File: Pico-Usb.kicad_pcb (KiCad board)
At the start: 2 copper layers, 25 x 60 mm, 40 parts, among them J1 USB_A, J3 MEM2067-02-180-00-A_REVB, J4 10133475-10001LF, SW1 SW_Push, SW2 SW_Push, SW3 SW_Push, SW4 A6H-4101, U1 RP2040, U2 W25Q128JVS, U3 MAX40200AUK, U4 MAX40200AUK, U5 AP2112K-3.3, U6 TS3USB221ARSER, Y2 ABM3B-12.000MHZ-10-1-U-T

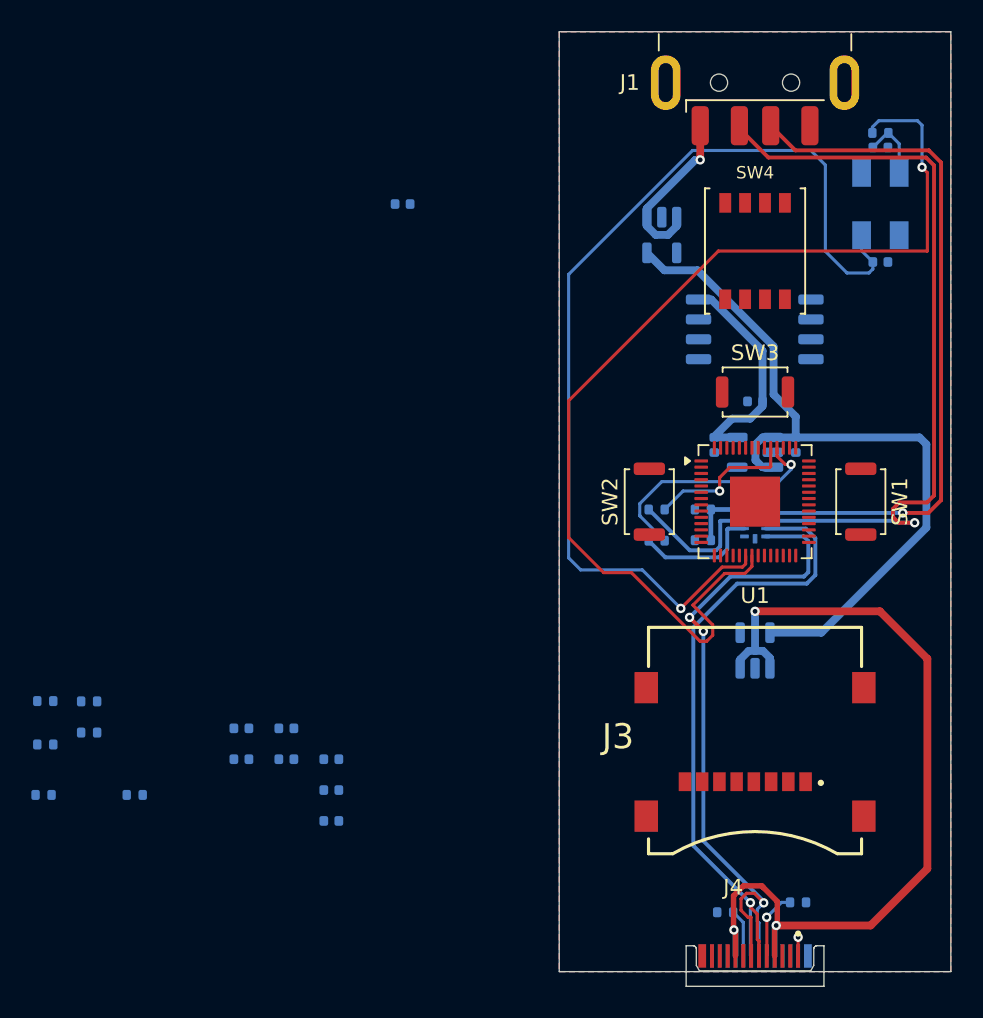
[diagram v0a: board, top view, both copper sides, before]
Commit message: Corregi el posicionamiento usb y mejore un poco la distribución de las pistas
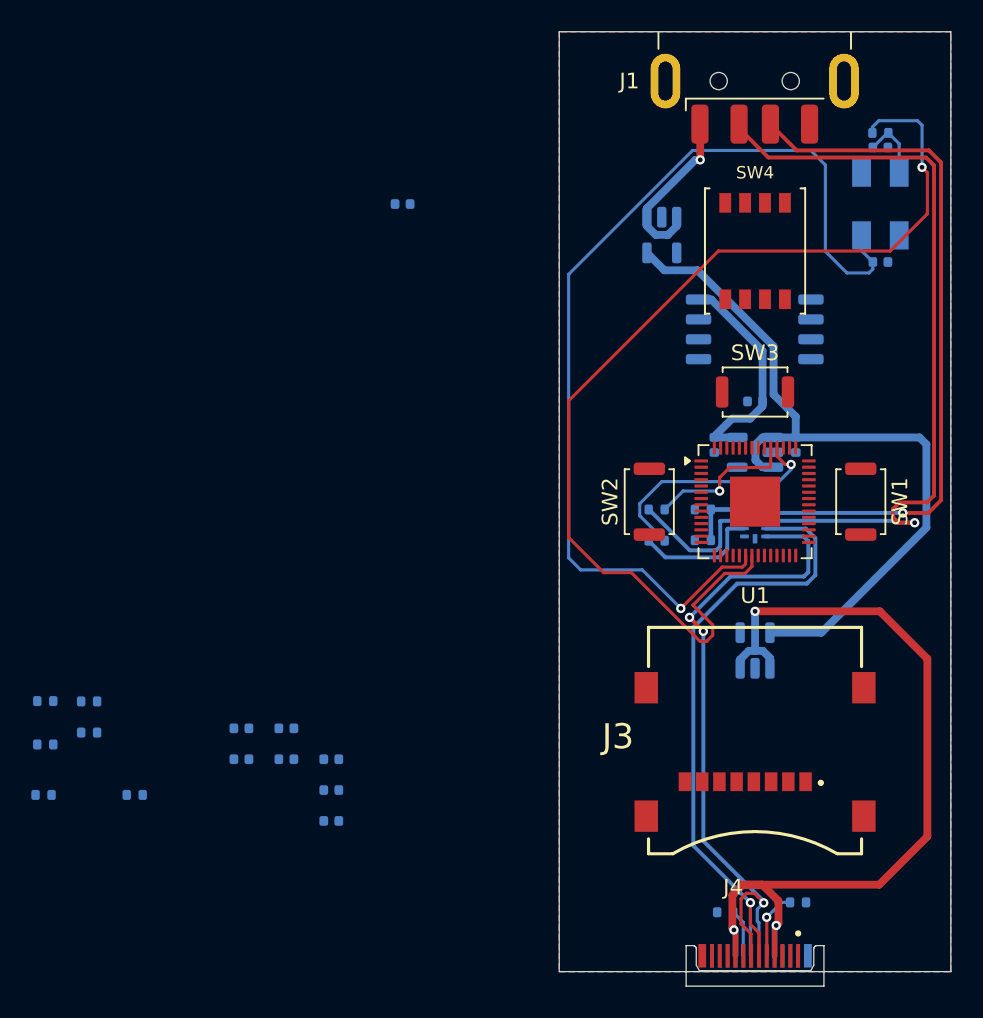
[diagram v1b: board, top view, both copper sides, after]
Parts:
- moved J1 0.10 mm to (137.5, 66.2)
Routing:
- net Net-(U1-XOUT): track 67.6 -> 66.2 mm
- net GNDREF: track 1.20 -> 0.00 mm, vias 1 -> 0

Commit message: Elimine todas las pistas y acomode los componetes
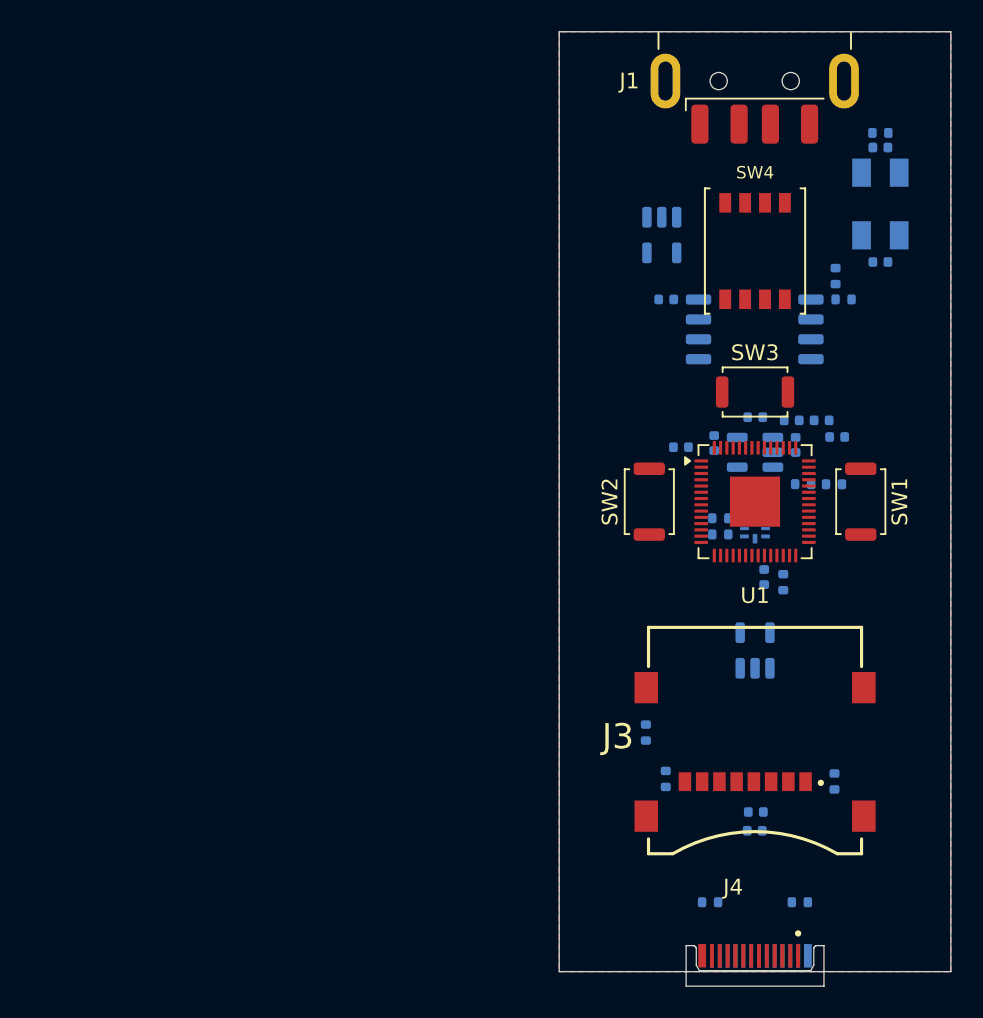
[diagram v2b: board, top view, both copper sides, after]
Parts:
- moved R6 55.5 mm to (143.2, 87.1), turned to 0 degrees
- moved R5 54.8 mm to (142.6, 85.6), turned to -90 degrees
- moved R13 50.5 mm to (142.6, 117.9), turned to -90 degrees
- moved R4 43.6 mm to (139.3, 105.1), turned to 90 degrees
- moved C5 40.5 mm to (142.7, 95.9), turned to 0 degrees
- moved R12 39.7 mm to (131.8, 117.7), turned to -90 degrees
- moved R11 38.4 mm to (130.5, 114.7), turned to -90 degrees
- moved C7 37.8 mm to (139.8, 94.8)
- moved C3 34.8 mm to (137.5, 94.6)
- moved C12 33.4 mm to (137.5, 121.0), turned to 0 degrees
- moved C13 33.0 mm to (137.6, 119.8), turned to 0 degrees
- moved C8 32.6 mm to (138.1, 104.8), turned to -90 degrees
- moved C4 31.3 mm to (132.8, 96.5)
- moved C6 30.1 mm to (141.8, 94.8), turned to 0 degrees
- moved R2 11.4 mm to (142.5, 98.9)
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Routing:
- net Net-(U1-XOUT): track 66.2 -> 0.00 mm, vias 1 -> 0
- net Net-(U1-XIN): track 64.2 -> 0.00 mm, vias 1 -> 0
- net VBUS_A: track 57.7 -> 0.00 mm, vias 3 -> 0
- net /USB_A_D-: track 49.5 -> 0.00 mm, vias 1 -> 0
- net /5V_Secure: track 48.6 -> 0.00 mm
- net /USB_A_D+: track 45.0 -> 0.00 mm, vias 1 -> 0
- net /USB_C_D-: track 43.2 -> 0.00 mm, vias 3 -> 0
- net /USB_C_D+: track 41.1 -> 0.00 mm, vias 1 -> 0
- net Net-(U1-USB_DM): track 15.6 -> 0.00 mm, vias 1 -> 0
- net /3.3V: track 14.4 -> 0.00 mm
- net Net-(J1-VBUS): track 11.0 -> 0.00 mm, vias 1 -> 0
- net Net-(U1-USB_DP): track 9.61 -> 0.00 mm, vias 1 -> 0
- net /MCU_D+: track 8.91 -> 0.00 mm
- net /MCU_D-: track 8.05 -> 0.00 mm
- net Net-(J4-CC1): track 4.35 -> 0.00 mm, vias 1 -> 0
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
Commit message: Elimine todas las pistas y acomode los componetes
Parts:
- renumbered SW2 to BOOTSEL, SW3 to MODE, SW1 to RST
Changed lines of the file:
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@@
 		(descr "http://www.alps.com/prod/info/E/HTML/Tact/SurfaceMount/SKRK/SKRKAHE020.html")
 		(tags "SMD SMT button")
-		(property "Reference" "SW3"
+		(property "Reference" "MODE"
 			(at 0 -2.5 0)
 			(layer "F.SilkS")
@@
 		(descr "http://www.alps.com/prod/info/E/HTML/Tact/SurfaceMount/SKRK/SKRKAHE020.html")
 		(tags "SMD SMT button")
-		(property "Reference" "SW1"
+		(property "Reference" "RST"
 			(at 0 -2.5 90)
 			(layer "F.SilkS")
@@
 		(descr "http://www.alps.com/prod/info/E/HTML/Tact/SurfaceMount/SKRK/SKRKAHE020.html")
 		(tags "SMD SMT button")
-		(property "Reference" "SW2"
+		(property "Reference" "BOOTSEL"
 			(at 0 -2.5 90)
 			(layer "F.SilkS")

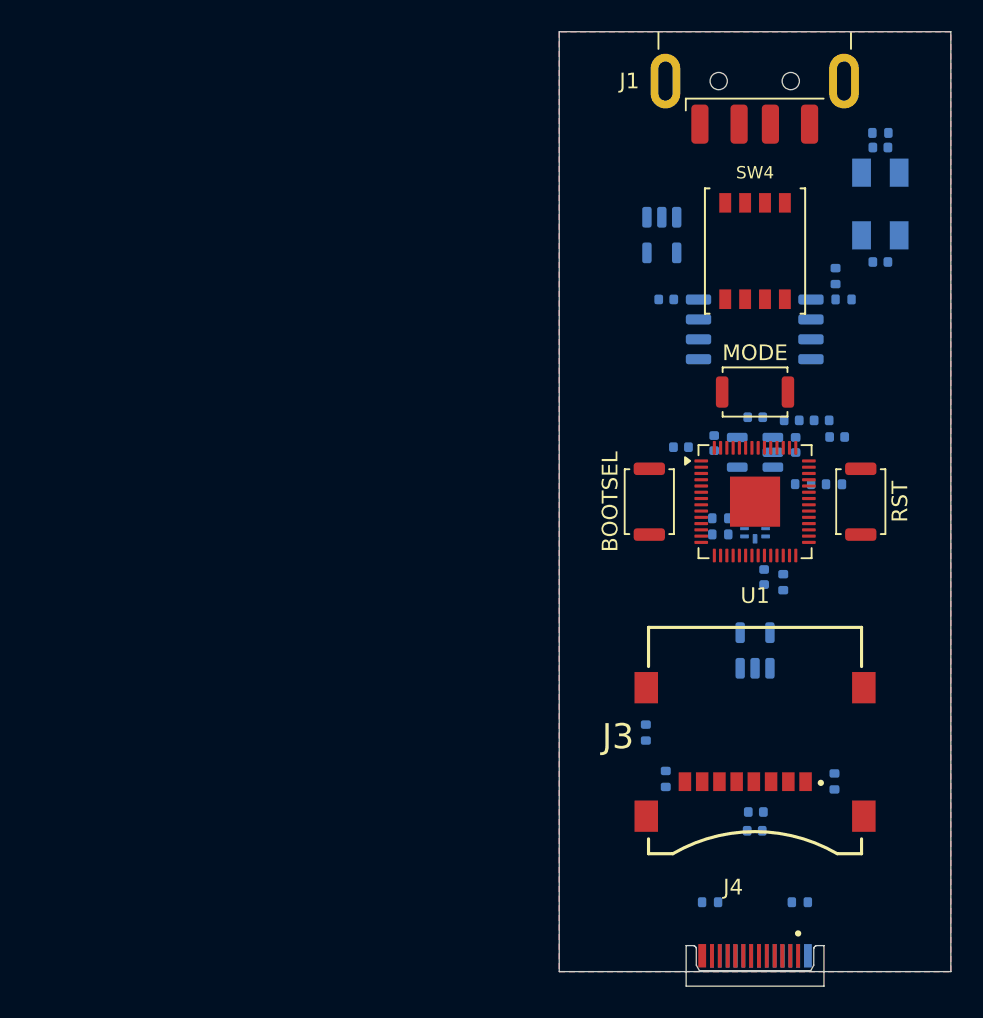
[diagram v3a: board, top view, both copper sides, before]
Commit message: Hice nuevo ruteo, checar y terminar o reiniciar por bloqueo de rutas para conexiones restantes
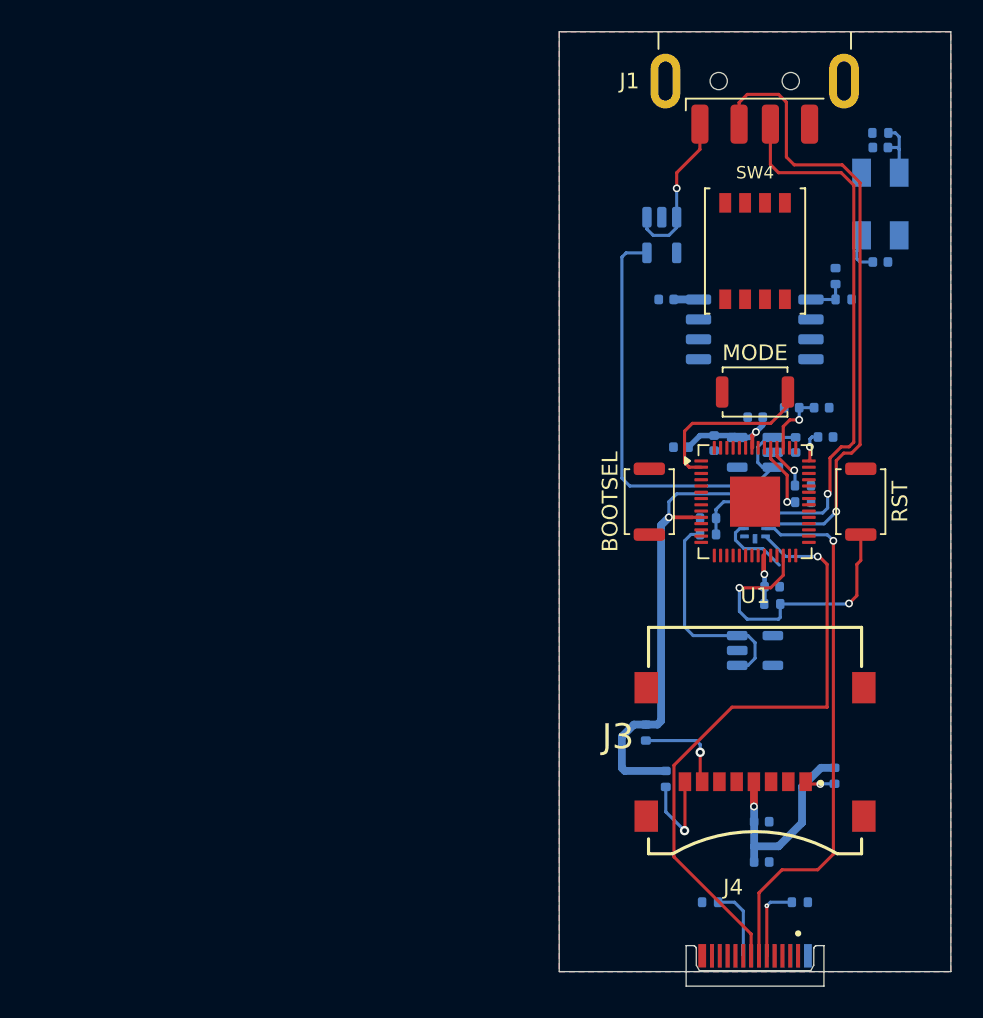
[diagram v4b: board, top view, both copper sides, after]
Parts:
- moved R2 2.28 mm to (140.6, 100.0), turned to 0 degrees
- moved C12 2.04 mm to (137.9, 123.0)
- moved R4 1.56 mm to (138.6, 106.5), turned to 0 degrees
- moved C6 0.81 mm to (141.8, 94.0)
- moved C7 0.81 mm to (139.8, 94.0)
- moved C8 0.80 mm to (138.6, 105.4), turned to 0 degrees
- moved R10 0.78 mm to (134.5, 101.1)
- moved R9 0.78 mm to (134.5, 102.1)
- moved C5 0.74 mm to (142.0, 95.9)
- moved C13 0.72 mm to (137.9, 120.4)
- moved R13 0.36 mm to (142.6, 117.5)
- moved R3 0.09 mm to (140.6, 99.0), turned to 180 degrees
- turned C1 to 0 degrees
- turned U4 to 0 degrees
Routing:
- net /3.3V: track 0.00 -> 58.0 mm, vias 0 -> 5
- net /USB_A_D-: track 0.00 -> 40.5 mm, vias 0 -> 1
- net /USB_C_D-: track 0.00 -> 39.3 mm, vias 0 -> 1
- net /USB_C_D+: track 0.00 -> 34.4 mm, vias 0 -> 1
- net /USB_A_D+: track 0.00 -> 34.1 mm, vias 0 -> 1
- net /5V_Secure: track 0.00 -> 30.9 mm
- net Net-(U1-RUN): track 0.00 -> 18.7 mm, vias 0 -> 2
- net VBUS_A: track 0.00 -> 13.9 mm
- net Net-(U1-GPIO0): track 0.00 -> 11.3 mm
- net Net-(J1-VBUS): track 0.00 -> 10.2 mm, vias 0 -> 1
- net Net-(J3-DAT1): track 0.00 -> 6.42 mm, vias 0 -> 1
- net /SPI_RX: track 0.00 -> 6.00 mm, vias 0 -> 1
- net Net-(J4-CC1): track 0.00 -> 4.88 mm, vias 0 -> 1
- net Net-(J4-CC2): track 0.00 -> 4.70 mm
- net /MCU_D-: track 0.00 -> 4.61 mm
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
